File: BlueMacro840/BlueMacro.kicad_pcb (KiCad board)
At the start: 4 copper layers, 20.3 x 48.3 mm, 33 parts, among them J1 Conn_01x02, J3 USB_C_Receptacle, Q1 SI2301CDS-T1-GE3, U1 TP4054ST, U2 E73-2G4M08S1C, U3 AP2112K-3.3, U4 Micro, U5 AP2112K-3.3, Y1 32.768kHz

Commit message: updates to BlueMacro840
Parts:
- C1, C2, C3, C4, C5, C6: footprint Capacitor_SMD:C_0402_1005Metric -> Capacitor_SMD:C_0603_1608Metric
- D2, D3, D4: footprint LED_SMD:LED_0402_1005Metric -> LED_SMD:LED_0603_1608Metric
- R1, R2, R3, R4, R5, R6, R7, R8, R9: footprint Resistor_SMD:R_0402_1005Metric -> Resistor_SMD:R_0603_1608Metric
- U3, U5: value AP2112K-3.3 -> AP2112K-3.3TRG1
- moved C3 10.5 mm to (50.3, 51.3)
- moved R8 9.70 mm to (53.3, 40.6)
- moved R7 9.70 mm to (43.2, 40.6)
- moved U5 9.66 mm to (44.2, 47.5)
- moved D4 8.94 mm to (53.3, 37.3)
- moved D3 8.94 mm to (43.2, 37.3)
- moved R2 5.66 mm to (43.2, 43.9), turned to 270 degrees
- moved R4 5.15 mm to (48.8, 43.9), turned to 270 degrees
- moved R6 4.53 mm to (45.0, 37.3), turned to 270 degrees
- moved R9 4.40 mm to (51.6, 37.3), turned to 270 degrees
- moved C6 3.85 mm to (47.0, 43.9), turned to 90 degrees
- moved C4 3.70 mm to (50.5, 43.9), turned to 90 degrees
- moved D2 3.64 mm to (45.0, 40.6)
- moved U1 3.00 mm to (47.8, 47.5)
- moved R5 2.94 mm to (50.5, 47.2), turned to 270 degrees
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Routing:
- net VBus: track 48.9 -> 67.5 mm
- net GND: track 120.4 -> 102.2 mm, vias 6 -> 7
- net BLUE_LED: track 50.8 -> 35.6 mm
- net SWO: track 34.8 -> 22.4 mm
- net VBatt_Monitor: track 17.7 -> 27.8 mm, vias 0 -> 2
- net /P0.05: track 16.1 -> 25.7 mm
- net /3V3: track 5.06 -> 14.6 mm
- net RED_LED: track 47.5 -> 38.4 mm
- net /P1.09: track 21.7 -> 30.7 mm
- net Net-(J3-PadB5): track 7.11 -> 12.5 mm
- net SWDCLK: track 7.18 -> 12.5 mm
- net Net-(J3-PadA5): track 7.19 -> 12.5 mm
- net Net-(C3-Pad1): track 24.0 -> 29.1 mm
- net Net-(R3-Pad1): track 1.66 -> 6.30 mm
- net Net-(R2-Pad2): track 1.61 -> 4.31 mm
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- added copper zone on B.Cu, net GND
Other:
- board text added: "0.02"
- board text added: "0.03"
- board text added: "0.04"
- board text added: "0.05"
- board text added: "0.06"
- board text added: "0.07"
- board text added: "0.08"
- board text added: "0.09"
- board text added: "0.10"
- board text added: "0.12"
- board text added: "0.13"
- board text added: "0.15"
- board text added: "0.17"
- board text added: "0.20"
- board text added: "0.22"
- board text added: "0.24"
- board text added: "0.26"
- board text added: "0.28"
- board text added: "0.29"
- board text added: "0.30"
- board text added: "1.06"
- board text added: "1.09"
- board text added: "1.11"
- board text added: "1.13"
- board text added: "3V3 Switched by P1.00"
- board text added: "5V Connected to VUSB"
- board text added: "BlueMacro840 1.0"
- board text added: "Footprint similar to Arduino Micro"
- board text added: "NC"
- board text added: "Vin Connected to VBatt"
- board text removed: "BlueMacro Footprint similar to Arduino Micro"

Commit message: adding BOM to Docs
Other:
- board text added: "VCC GND CK IO"
- board text removed: "VCC GND IO CK"
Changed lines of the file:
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@@
   )
   (setup
-    (last_trace_width 0.2)
+    (last_trace_width 0.25)
     (user_trace_width 0.2)
     (trace_clearance 0.2)
@@
   (gr_line (start 39.624 46.482) (end 39.624 58.801) (layer B.SilkS) (width 0.2))
   (gr_line (start 38.227 46.482) (end 39.624 46.482) (layer B.SilkS) (width 0.2))
-  (gr_text "VCC GND IO CK" (at 38.989 52.451 90) (layer B.SilkS)
+  (gr_text "VCC GND CK IO" (at 38.989 52.451 90) (layer B.SilkS)
     (effects (font (size 1 1) (thickness 0.1)) (justify mirror))
   )

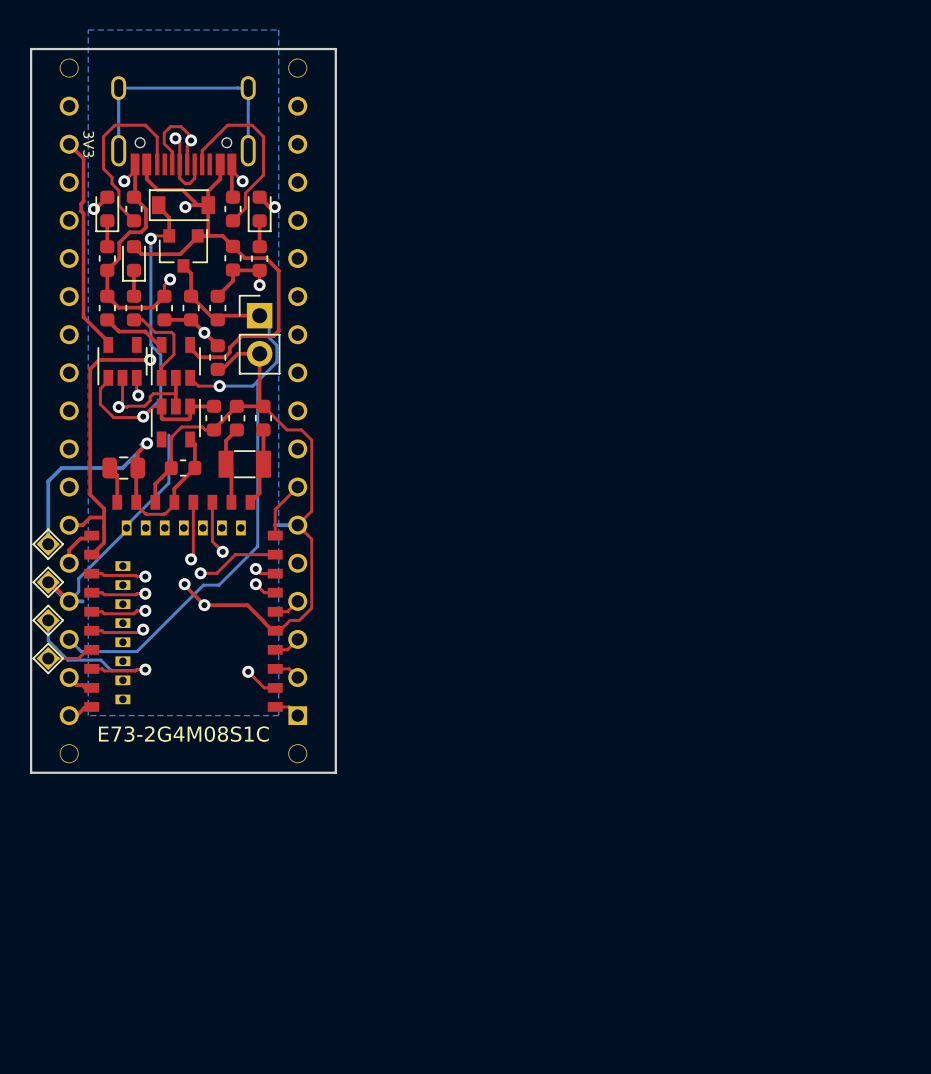
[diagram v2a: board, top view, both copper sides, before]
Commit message: fixed bluemacro840 schematic in docs
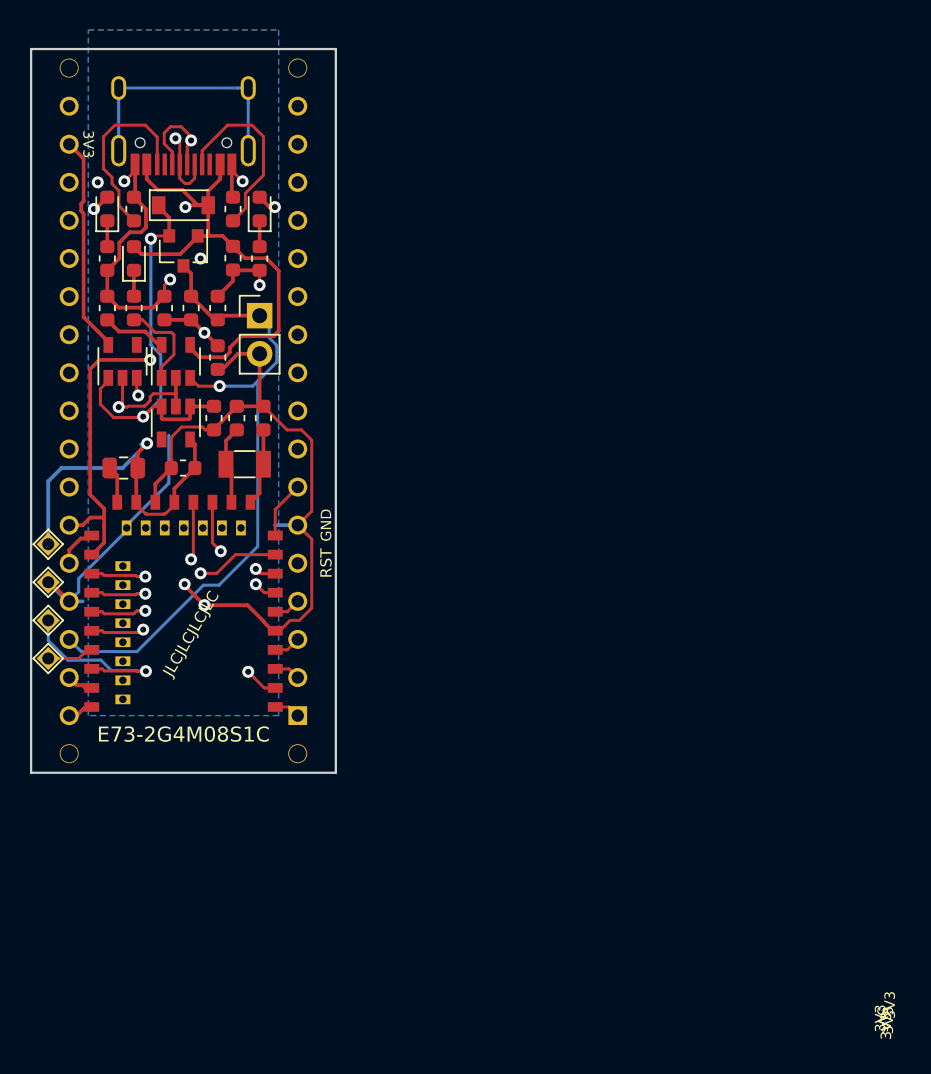
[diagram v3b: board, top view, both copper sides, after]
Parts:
- added ?: , , F.Cu at (63.2, 54.2)
- added ?: , , F.Cu at (54.6, 60.7)
- added ?: , , F.Cu at (42.0, 31.5)
- added ?: , , F.Cu at (41.9, 32.5)
- added ?: , , F.Cu at (36.8, 32.5)
- added ?: , , F.Cu at (41.8, 32.9)
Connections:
- U2 pad 38: (no net) -> /P1.02
- U4 pad 15: /P0.04 -> /P1.06
- U4 pad 17: /P1.06 -> /P1.02
- U4 pad 20: (no net) -> /P0.04
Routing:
- net /P1.02: track 0.00 -> 45.6 mm
- net /P1.06: track 47.8 -> 40.4 mm
- net /P0.04: track 27.2 -> 29.3 mm, vias 0 -> 2
- net /P1.09: track 30.7 -> 30.2 mm
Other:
- board text added: "1.02"
- board text added: "BlueMacro840 2.0"
- board text added: "JLCJLCJLCJLC"
- board text added: "RST"
- board text removed: "BlueMacro840 1.0"
